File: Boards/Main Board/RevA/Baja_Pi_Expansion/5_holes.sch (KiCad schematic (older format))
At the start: 5 parts

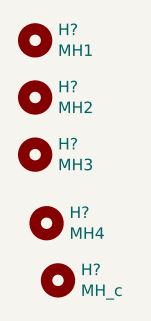
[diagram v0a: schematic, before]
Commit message: Added a Majority of Main Board Footprints
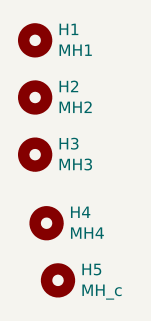
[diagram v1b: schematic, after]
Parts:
- H1, H2, H3, H4, H5: renamed from H?; footprint (none) -> MountingHole:MountingHole_2.7mm_M2.5
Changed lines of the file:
@@
 U 1 1 616656F1
 P 4350 3050
-F 0 "H?" H 4450 3096 50  0000 L CNN
+AR Path="/616656F1" Ref="H?"  Part="1"
+AR Path="/61664AB6/616656F1" Ref="H1"  Part="1"
+F 0 "H1" H 4450 3096 50  0000 L CNN
 F 1 "MH1" H 4450 3005 50  0000 L CNN
-F 2 "" H 4350 3050 50  0001 C CNN
+F 2 "MountingHole:MountingHole_2.7mm_M2.5" H 4350 3050 50  0001 C CNN
 F 3 "~" H 4350 3050 50  0001 C CNN
 	1    4350 3050
@@
 U 1 1 616656F7
 P 4350 3300
-F 0 "H?" H 4450 3346 50  0000 L CNN
+AR Path="/616656F7" Ref="H?"  Part="1"
+AR Path="/61664AB6/616656F7" Ref="H2"  Part="1"
+F 0 "H2" H 4450 3346 50  0000 L CNN
 F 1 "MH2" H 4450 3255 50  0000 L CNN
-F 2 "" H 4350 3300 50  0001 C CNN
+F 2 "MountingHole:MountingHole_2.7mm_M2.5" H 4350 3300 50  0001 C CNN
 F 3 "~" H 4350 3300 50  0001 C CNN
 	1    4350 3300
@@
 U 1 1 616656FD
 P 4350 3550
-F 0 "H?" H 4450 3596 50  0000 L CNN
+AR Path="/616656FD" Ref="H?"  Part="1"
+AR Path="/61664AB6/616656FD" Ref="H3"  Part="1"
+F 0 "H3" H 4450 3596 50  0000 L CNN
 F 1 "MH3" H 4450 3505 50  0000 L CNN
-F 2 "" H 4350 3550 50  0001 C CNN
+F 2 "MountingHole:MountingHole_2.7mm_M2.5" H 4350 3550 50  0001 C CNN
 F 3 "~" H 4350 3550 50  0001 C CNN
 	1    4350 3550
@@
 U 1 1 61665703
 P 4400 3850
-F 0 "H?" H 4500 3896 50  0000 L CNN
+AR Path="/61665703" Ref="H?"  Part="1"
+AR Path="/61664AB6/61665703" Ref="H4"  Part="1"
+F 0 "H4" H 4500 3896 50  0000 L CNN
 F 1 "MH4" H 4500 3805 50  0000 L CNN
-F 2 "" H 4400 3850 50  0001 C CNN
+F 2 "MountingHole:MountingHole_2.7mm_M2.5" H 4400 3850 50  0001 C CNN
 F 3 "~" H 4400 3850 50  0001 C CNN
 	1    4400 3850
@@
 U 1 1 61665709
 P 4450 4100
-F 0 "H?" H 4550 4146 50  0000 L CNN
+AR Path="/61665709" Ref="H?"  Part="1"
+AR Path="/61664AB6/61665709" Ref="H5"  Part="1"
+F 0 "H5" H 4550 4146 50  0000 L CNN
 F 1 "MH_c" H 4550 4055 50  0000 L CNN
-F 2 "" H 4450 4100 50  0001 C CNN
+F 2 "MountingHole:MountingHole_2.7mm_M2.5" H 4450 4100 50  0001 C CNN
 F 3 "~" H 4450 4100 50  0001 C CNN
 	1    4450 4100
